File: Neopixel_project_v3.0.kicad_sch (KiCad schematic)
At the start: 67 parts, among them J1 USB_C_Receptacle_USB2.0_16P, J2 Conn_01x02_Pin, Q1 MMBT3904, Q2 MMBT3904, Q3 MMBT3904, Q4 MMBT3904, Q5 DO3407B, Q6 DO3407B, Q7 DO3407B, Q8 DO3407B, SW1 SW_Push, SW2 SW_Push, U1 ESP8685H4, U2 AL8843, U4 USBLC6-4SC6, U5 MC34063AD, Y1 Crystal_GND24

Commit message: changes
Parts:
- removed C1: 100µF, Capacitor_SMD:C_0603_1608Metric, symbol Device:C
- removed C14, C2: 100µF, symbol Device:C
- removed D6: SS34, Diode_SMD:D_SMA, symbol Device:D
- removed SW1, SW2: SW_Push, symbol Switch:SW_Push
- removed U5: MC34063AD, Package_SO:SOIC-8_3.9x4.9mm_P1.27mm, symbol Regulator_Switching:MC34063AD
- added C1, C14, C2: 100µF, Capacitor_SMD:CP_Elec_6.3x7.7, symbol Device:C_Polarized
- added SW1, SW2: TS-1088-AR02016, TS-1088-AR02016:SW_TS-1088_XNP, symbol TS-1088-AR02016:TS-1088-AR02016
- added U3: TD1469, symbol mylibrary:TD1469
- C10, C11, C12, C4, C6, C7, C9: footprint (none) -> Capacitor_SMD:C_0603_1608Metric
- C13: value 7.8µF -> 100nF; footprint (none) -> Capacitor_SMD:C_0603_1608Metric
- C15, C16, C8: footprint (none) -> Capacitor_SMD:C_0805_2012Metric
- C17, C18, C5: footprint (none) -> Capacitor_SMD:C_0402_1005Metric
- C19, C20: footprint (none) -> Capacitor_SMD:C_0402_1005Metric; now not fitted
- C3: footprint Capacitor_SMD:C_0603_1608Metric -> Capacitor_SMD:C_0805_2012Metric
- L1: value 68µ -> 68µH
- L2, L4: footprint (none) -> Inductor_SMD:L_0603_1608Metric
- L3: value 5.6µH -> 22µH; footprint (none) -> Inductor_SMD:L_Ferrocore_DLG-0302
- L5: footprint (none) -> Inductor_SMD:L_0402_1005Metric
- R1, R3, R5, R7: footprint (none) -> Resistor_SMD:R_2010_5025Metric
- R10, R11, R12, R13, R14, R9: footprint (none) -> Resistor_SMD:R_0603_1608Metric
- R15: value 0.333 -> 1M; footprint (none) -> Resistor_SMD:R_0603_1608Metric
- R16: value 2k2 -> 16k; footprint (none) -> Resistor_SMD:R_0603_1608Metric
- R17: value 3k6 -> 5.1k; footprint (none) -> Resistor_SMD:R_0603_1608Metric
- R2, R4, R6, R8: footprint (none) -> Resistor_SMD:R_1206_3216Metric
- U1: footprint (none) -> ESP8685:QFN284X4_EXP
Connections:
- net 24V: now also C1.1, C2.1, U3. (VIN)
- net 3v3: now also R16.2, C14.1; no longer R17.1
- net BOOT: now also SW1.2
- net CHIP_EN: now also SW2.2
- net GND: now also R17.2, C1.2, C14.2, C2.2, SW1.1, SW2.1, U3. (VIN); no longer C13.2, R16.1
- net at R15.2: now also U3. (VIN)
- net at L3.1: now also C13.2, U3. (VIN)
- net at C13.1: now also U3. (VIN)
- new net: R16.1, R17.1, U3. (VIN)
- no-connect marks 11 -> 12
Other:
- note removed: "Tc=4.0 * 10-5 * ton"
- note removed: "Ton=0.195 μs"
- note removed: "Vf=0.55v"
- note removed: "Vout=1.25(1+(R16/R17))"
- moved on the sheet: C11, C12, C15, C16, J1, R10, R13, R14, R9, U4

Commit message: changes
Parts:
- J1: footprint (none) -> Connector_USB:USB_C_Receptacle_G-Switch_GT-USB-7051x
- J2: footprint (none) -> Connector_AMASS:AMASS_XT30UPB-M_1x02_P5.0mm_Vertical
- U3: footprint (none) -> Package_TO_SOT_SMD:TSOT-23-6
- Y1: footprint (none) -> Crystal:Crystal_SMD_Abracon_ABM8AIG-4Pin_3.2x2.5mm
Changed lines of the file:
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@@
 			)
 		)
-		(property "Footprint" ""
+		(property "Footprint" "Package_TO_SOT_SMD:TSOT-23-6"
 			(at 229.87 39.37 0)
 			(effects
@@
 			)
 		)
-		(property "Footprint" ""
+		(property "Footprint" "Crystal:Crystal_SMD_Abracon_ABM8AIG-4Pin_3.2x2.5mm"
 			(at 111.76 172.72 0)
 			(effects
@@
 			)
 		)
-		(property "Footprint" ""
+		(property "Footprint" "Connector_USB:USB_C_Receptacle_G-Switch_GT-USB-7051x"
 			(at 142.24 43.18 0)
 			(effects
@@
 			)
 		)
-		(property "Footprint" ""
+		(property "Footprint" "Connector_AMASS:AMASS_XT30UPB-M_1x02_P5.0mm_Vertical"
 			(at 27.94 82.55 0)
 			(effects

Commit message: snapshot save
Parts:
- removed J1: USB_C_Receptacle_USB2.0_16P, Connector_USB:USB_C_Receptacle_G-Switch_GT-USB-7051x, symbol Connector:USB_C_Receptacle_USB2.0_16P
- removed R13, R14: 5k1, Resistor_SMD:R_0603_1608Metric, symbol Device:R
- added J1: Conn_01x03_Pin, Connector_PinHeader_2.54mm:PinHeader_1x03_P2.54mm_Vertical, symbol Connector:Conn_01x03_Pin
- R1, R3, R5, R7: value 1k -> 1k5; footprint Resistor_SMD:R_2010_5025Metric -> Resistor_SMD:R_1206_3216Metric
- R17: value 5.1k -> 5k1
- R2, R4, R6, R8: footprint Resistor_SMD:R_1206_3216Metric -> Resistor_SMD:R_0805_2012Metric
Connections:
- net 24V: now also U3.5 (VIN); no longer U3. (VIN)
- net GND: now also U3.2 (GND), J1.1 (Pin_1); no longer U3. (VIN)
- net USB_D+: now also J1.3 (Pin_3)
- net USB_D-: now also J1.2 (Pin_2)
- net at R16.1, R17.1: now also U3.3 (FB); no longer U3. (VIN)
- net at C13.2, L3.1: now also U3.6 (SW); no longer U3. (VIN)
- net at R15.2: now also U3.4 (EN); no longer U3. (VIN)
- net at C13.1: now also U3.1 (BST); no longer U3. (VIN)
- no-connect marks 12 -> 8

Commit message: pcb finished
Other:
- note added: "Programming_pins"
- note removed: "usb_connector"
- moved on the sheet: J1, U4
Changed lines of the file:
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@@
 	)
 	(no_connect
-		(at 172.72 53.34)
+		(at 160.02 40.64)
 	)
 	(no_connect
@@
 	)
 	(no_connect
-		(at 175.26 53.34)
+		(at 162.56 40.64)
 	)
 	(no_connect
@@
 	(wire
 		(pts
-			(xy 149.86 50.8) (xy 167.64 50.8)
+			(xy 137.16 38.1) (xy 154.94 38.1)
 		)
 		(stroke
@@
 	(wire
 		(pts
-			(xy 158.75 60.96) (xy 162.56 60.96)
+			(xy 146.05 48.26) (xy 149.86 48.26)
 		)
 		(stroke
@@
 	(wire
 		(pts
-			(xy 149.86 48.26) (xy 170.18 48.26)
+			(xy 137.16 35.56) (xy 157.48 35.56)
 		)
 		(stroke
@@
 	(wire
 		(pts
-			(xy 154.94 45.72) (xy 154.94 39.37)
+			(xy 142.24 33.02) (xy 142.24 26.67)
 		)
 		(stroke
@@
 	(wire
 		(pts
-			(xy 167.64 50.8) (xy 167.64 53.34)
+			(xy 154.94 38.1) (xy 154.94 40.64)
 		)
 		(stroke
@@
 	(wire
 		(pts
-			(xy 158.75 66.04) (xy 158.75 60.96)
+			(xy 146.05 53.34) (xy 146.05 48.26)
 		)
 		(stroke
@@
 	(wire
 		(pts
-			(xy 170.18 48.26) (xy 170.18 53.34)
+			(xy 157.48 35.56) (xy 157.48 40.64)
 		)
 		(stroke
@@
 	(wire
 		(pts
-			(xy 149.86 45.72) (xy 154.94 45.72)
+			(xy 137.16 33.02) (xy 142.24 33.02)
 		)
 		(stroke
@@
 		)
 	)
-	(text "usb_connector"
+	(text "Programming_pins"
 		(exclude_from_sim no)
 		(at 143.764 16.764 0)
@@
 	(global_label "USB_D+"
 		(shape input)
-		(at 167.64 53.34 180)
+		(at 154.94 40.64 180)
 		(fields_autoplaced yes)
 		(effects
@@
 		)
 		(property "Intersheetrefs" "${INTERSHEET_REFS}"
-			(at 157.0348 53.34 0)
+			(at 144.3348 40.64 0)
 			(effects
 				(font
@@
 	(global_label "3v3"
 		(shape input)
-		(at 180.34 60.96 0)
+		(at 167.64 48.26 0)
 		(fields_autoplaced yes)
 		(effects
@@
 		)
 		(property "Intersheetrefs" "${INTERSHEET_REFS}"
-			(at 186.7118 60.96 0)
+			(at 174.0118 48.26 0)
 			(effects
 				(font
@@
 	(global_label "USB_D-"
 		(shape input)
-		(at 170.18 48.26 0)
+		(at 157.48 35.56 0)
 		(fields_autoplaced yes)
 		(effects
@@
 		)
 		(property "Intersheetrefs" "${INTERSHEET_REFS}"
-			(at 180.7852 48.26 0)
+			(at 168.0852 35.56 0)
 			(effects
 				(font
@@
 	(symbol
 		(lib_id "Connector:Conn_01x03_Pin")
-		(at 144.78 48.26 0)
+		(at 132.08 35.56 0)
 		(unit 1)
 		(exclude_from_sim no)
@@
 		(fields_autoplaced yes)
 		(property "Reference" "J1"
-			(at 145.415 40.64 0)
+			(at 132.715 27.94 0)
 			(effects
 				(font
@@
 		)
 		(property "Value" "Conn_01x03_Pin"
-			(at 145.415 43.18 0)
+			(at 132.715 30.48 0)
 			(effects
 				(font
@@
 		)
 		(property "Footprint" "Connector_PinHeader_2.54mm:PinHeader_1x03_P2.54mm_Vertical"
-			(at 144.78 48.26 0)
+			(at 132.08 35.56 0)
 			(effects
 				(font
@@
 		)
 		(property "Datasheet" "~"
-			(at 144.78 48.26 0)
+			(at 132.08 35.56 0)
 			(effects
 				(font
@@
 		)
 		(property "Description" "Generic connector, single row, 01x03, script generated"
-			(at 144.78 48.26 0)
+			(at 132.08 35.56 0)
 			(effects
 				(font
@@
 	(symbol
 		(lib_id "power:GND")
-		(at 158.75 66.04 0)
+		(at 146.05 53.34 0)
 		(unit 1)
 		(exclude_from_sim no)
@@
 		(dnp no)
 		(property "Reference" "#PWR026"
-			(at 158.75 72.39 0)
+			(at 146.05 59.69 0)
 			(effects
 				(font
@@
 		)
 		(property "Value" "GND"
-			(at 160.782 66.294 0)
+			(at 148.082 53.594 0)
 			(effects
 				(font
@@
 		)
 		(property "Footprint" ""
-			(at 158.75 66.04 0)
+			(at 146.05 53.34 0)
 			(effects
 				(font
@@
 		)
 		(property "Datasheet" ""
-			(at 158.75 66.04 0)
+			(at 146.05 53.34 0)
 			(effects
 				(font
@@
 		)
 		(property "Description" "Power symbol creates a global label with name \"GND\" , ground"
-			(at 158.75 66.04 0)
+			(at 146.05 53.34 0)
 			(effects
 				(font
@@
 	(symbol
 		(lib_id "Power_Protection:USBLC6-4SC6")
-		(at 172.72 60.96 270)
+		(at 160.02 48.26 270)
 		(unit 1)
 		(exclude_from_sim no)
@@
 		(dnp no)
 		(property "Reference" "U4"
-			(at 170.18 69.088 90)
+			(at 157.48 56.388 90)
 			(effects
 				(font
@@
 		)
 		(property "Value" "USBLC6-4SC6"
-			(at 165.1 66.802 90)
+			(at 152.4 54.102 90)
 			(effects
 				(font
@@
 		)
 		(property "Footprint" "Package_TO_SOT_SMD:SOT-23-6"
-			(at 162.56 63.5 0)
+			(at 149.86 50.8 0)
 			(effects
 				(font
@@
 		)
 		(property "Datasheet" "https://www.st.com/resource/en/datasheet/usblc6-4.pdf"
-			(at 160.02 63.5 0)
+			(at 147.32 50.8 0)
 			(effects
 				(font
@@
 		)
 		(property "Description" "Very low capacitance ESD protection diode, 4 data-line, SOT-23-6"
-			(at 172.72 60.96 0)
+			(at 160.02 48.26 0)
 			(effects
 				(font
@@
 	(symbol
 		(lib_id "power:GND")
-		(at 154.94 39.37 180)
+		(at 142.24 26.67 180)
 		(unit 1)
 		(exclude_from_sim no)
@@
 		(dnp no)
 		(property "Reference" "#PWR020"
-			(at 154.94 33.02 0)
+			(at 142.24 20.32 0)
 			(effects
 				(font
@@
 		)
 		(property "Value" "GND"
-			(at 152.908 39.116 0)
+			(at 140.208 26.416 0)
 			(effects
 				(font
@@
 		)
 		(property "Footprint" ""
-			(at 154.94 39.37 0)
+			(at 142.24 26.67 0)
 			(effects
 				(font
@@
 		)
 		(property "Datasheet" ""
-			(at 154.94 39.37 0)
+			(at 142.24 26.67 0)
 			(effects
 				(font
@@
 		)
 		(property "Description" "Power symbol creates a global label with name \"GND\" , ground"
-			(at 154.94 39.37 0)
+			(at 142.24 26.67 0)
 			(effects
 				(font

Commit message: pcb and 3d models finished
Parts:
- removed J2: Conn_01x02_Pin, Connector_AMASS:AMASS_XT30UPB-M_1x02_P5.0mm_Vertical, symbol Connector:Conn_01x02_Pin
- added J3: Screw_Terminal_01x02, TerminalBlock_Phoenix:TerminalBlock_Phoenix_MPT-0,5-2-2.54_1x02_P2.54mm_Horizontal, symbol Connector:Screw_Terminal_01x02
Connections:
- net 24V: now also J3.2 (Pin_2)
- net GND: now also J3.1 (Pin_1)
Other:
- note removed: "checklist: - confirm circuit wiring - check available components and cart - make sure no unensesarry components are in the cart - confirm custom schematic symbol pin numbers - confirm footprints - confirm footprint pinouts"
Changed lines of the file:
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@@
 	(wire
 		(pts
-			(xy 33.02 88.9) (xy 33.02 85.09)
-		)
-		(stroke
-			(width 0)
-			(type default)
-		)
-	)
-	(wire
-		(pts
 			(xy 153.67 158.75) (xy 181.61 158.75)
 		)
@@
 	(wire
 		(pts
-			(xy 33.02 82.55) (xy 38.1 82.55)
-		)
-		(stroke
-			(width 0)
-			(type default)
-		)
-	)
-	(wire
-		(pts
 			(xy 196.85 101.6) (xy 213.36 101.6)
 		)
@@
 		)
 	)
-	(text "checklist:\n- confirm circuit wiring\n- check available components and cart\n- make sure no unensesarry components are in the cart\n- confirm custom schematic symbol pin numbers\n- confirm footprints\n- confirm footprint pinouts\n"
-		(exclude_from_sim no)
-		(at 10.16 -34.29 0)
-		(effects
-			(font
-				(size 5.08 5.08)
-			)
-			(justify left)
-		)
-	)
 	(text "led_circuit"
 		(exclude_from_sim no)
@@
 	(global_label "24V"
 		(shape input)
-		(at 38.1 82.55 0)
+		(at 34.29 83.82 0)
 		(fields_autoplaced yes)
 		(effects
@@
 		)
 		(property "Intersheetrefs" "${INTERSHEET_REFS}"
-			(at 44.5928 82.55 0)
+			(at 40.7828 83.82 0)
 			(effects
 				(font
@@
 	(symbol
 		(lib_id "power:GND")
-		(at 33.02 88.9 0)
+		(at 34.29 86.36 0)
 		(unit 1)
 		(exclude_from_sim no)
@@
 		(fields_autoplaced yes)
 		(property "Reference" "#PWR036"
-			(at 33.02 95.25 0)
+			(at 34.29 92.71 0)
 			(effects
 				(font
@@
 		)
 		(property "Value" "GND"
-			(at 33.02 93.98 0)
+			(at 34.29 91.44 0)
 			(effects
 				(font
@@
 		)
 		(property "Footprint" ""
-			(at 33.02 88.9 0)
+			(at 34.29 86.36 0)
 			(effects
 				(font
@@
 		)
 		(property "Datasheet" ""
-			(at 33.02 88.9 0)
+			(at 34.29 86.36 0)
 			(effects
 				(font
@@
 		)
 		(property "Description" "Power symbol creates a global label with name \"GND\" , ground"
-			(at 33.02 88.9 0)
+			(at 34.29 86.36 0)
 			(effects
 				(font
@@
 	)
 	(symbol
+		(lib_id "Connector:Screw_Terminal_01x02")
+		(at 29.21 86.36 180)
+		(unit 1)
+		(exclude_from_sim no)
+		(in_bom yes)
+		(on_board yes)
+		(dnp no)
+		(fields_autoplaced yes)
+		(property "Reference" "J3"
+			(at 29.21 77.47 0)
+			(effects
+				(font
+					(size 1.27 1.27)
+				)
+			)
+		)
+		(property "Value" "Screw_Terminal_01x02"
+			(at 29.21 80.01 0)
+			(effects
+				(font
+					(size 1.27 1.27)
+				)
+			)
+		)
+		(property "Footprint" "TerminalBlock_Phoenix:TerminalBlock_Phoenix_MPT-0,5-2-2.54_1x02_P2.54mm_Horizontal"
+			(at 29.21 86.36 0)
+			(effects
+				(font
+					(size 1.27 1.27)
+				)
+				(hide yes)
+			)
+		)
+		(property "Datasheet" "~"
+			(at 29.21 86.36 0)
+			(effects
+				(font
+					(size 1.27 1.27)
+				)
+				(hide yes)
+			)
+		)
+		(property "Description" "Generic screw terminal, single row, 01x02, script generated (kicad-library-utils/schlib/autogen/connector/)"
+			(at 29.21 86.36 0)
+			(effects
+				(font
+					(size 1.27 1.27)
+				)
+				(hide yes)
+			)
+		)
+		(pin "2"
+		)
+		(pin "1"
+		)
+		(instances
+			(project "Neopixel_project_v3.0"
+				(path "/b6956c8d-1b4a-4d29-b075-b5f8d692fa3c"
+					(reference "J3")
+					(unit 1)
+				)
+			)
+		)
+	)
+	(symbol
 		(lib_id "Transistor_BJT:MMBT3904")
 		(at 151.13 111.76 0)
@@
 					(unit 1)
 				)
-			)
-		)
-	)
-	(symbol
-		(lib_id "Connector:Conn_01x02_Pin")
-		(at 27.94 82.55 0)
-		(unit 1)
-		(exclude_from_sim no)
-		(in_bom yes)
-		(on_board yes)
-		(dnp no)
-		(fields_autoplaced yes)
-		(property "Reference" "J2"
-			(at 28.575 77.47 0)
-			(effects
-				(font
-					(size 1.27 1.27)
-				)
-			)
-		)
-		(property "Value" "Conn_01x02_Pin"
-			(at 28.575 80.01 0)
-			(effects
-				(font
-					(size 1.27 1.27)
-				)
-			)
-		)
-		(property "Footprint" "Connector_AMASS:AMASS_XT30UPB-M_1x02_P5.0mm_Vertical"
-			(at 27.94 82.55 0)
-			(effects
-				(font
-					(size 1.27 1.27)
-				)
-				(hide yes)
-			)
-		)
-		(property "Datasheet" "~"
-			(at 27.94 82.55 0)
-			(effects
-				(font
-					(size 1.27 1.27)
-				)
-				(hide yes)
-			)
-		)
-		(property "Description" "Generic connector, single row, 01x02, script generated"
-			(at 27.94 82.55 0)
-			(effects
-				(font
-					(size 1.27 1.27)
-				)
-				(hide yes)
-			)
-		)
-		(pin "1"
-		)
-		(pin "2"
-		)
-		(instances
-			(project "Neopixel_project_v3.0"
-				(path "/b6956c8d-1b4a-4d29-b075-b5f8d692fa3c"
-					(reference "J2")
-					(unit 1)
-				)

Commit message: added bom.csv and buch of other changes
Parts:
- AE1: now left out of the parts list
- C1, C14, C2: PPU (none) -> 0.0193
- C10, C11, C12, C13, C6, C7, C9: PPU (none) -> 0.0021
- C15, C16, C3: PPU (none) -> 0.1158
- C17, C18: PPU (none) -> 0.0033
- C19, C20: PPU (none) -> 0
- C4: PPU (none) -> 0.0038
- C5, R10, R17, R9: PPU (none) -> 0.0009
- C8: PPU (none) -> 0.0178
- D1: PPU (none) -> 0.069
- D2: PPU (none) -> 0.1638
- D3: PPU (none) -> 0.1589
- D4: PPU (none) -> 0.0962
- D5: PPU (none) -> 0.0265
- J1: PPU (none) -> 0.0105
- J3: PPU (none) -> 0.1513
- L1: PPU (none) -> 0.052
- L2: PPU (none) -> 0.0069
- L3: PPU (none) -> 0.0184
- L4: PPU (none) -> 0.0064
- L5: PPU (none) -> 0.0006
- Q1, Q2, Q3, Q4: PPU (none) -> 0.0095
- Q5, Q6, Q7, Q8: PPU (none) -> 0.0271
- R1, R3, R5, R7: PPU (none) -> 0.013
- R11, R12: value 10k -> 5k1; PPU (none) -> 0.0009
- R15: PPU (none) -> 0.001
- R16: PPU (none) -> 0.0012
- R2, R4, R6, R8: PPU (none) -> 0.0156
- R22: PPU (none) -> 0.0488
- SW1, SW2: PPU (none) -> 0.0415
- U1: PPU (none) -> 1.3435
- U2: PPU (none) -> 0.3568
- U3: PPU (none) -> 0.2999
- U4: PPU (none) -> 0.0273
- Y1: PPU (none) -> 0.0922

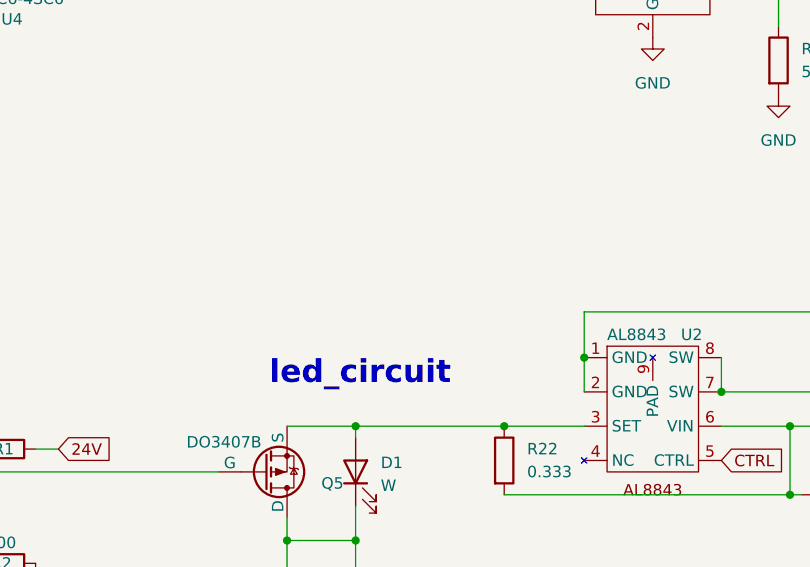
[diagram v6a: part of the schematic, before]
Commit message: added heatsink to bom
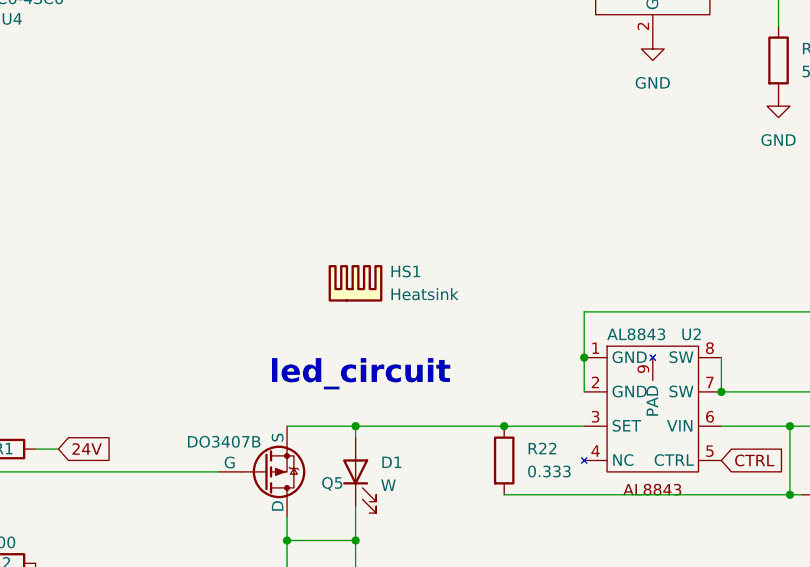
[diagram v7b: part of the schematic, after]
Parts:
- added HS1: Heatsink, 22x22x10, symbol Mechanical:Heatsink
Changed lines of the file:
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@@
+	)
+	(symbol
+		(lib_id "Mechanical:Heatsink")
+		(at 196.85 87.63 0)
+		(unit 1)
+		(exclude_from_sim yes)
+		(in_bom yes)
+		(on_board no)
+		(dnp no)
+		(fields_autoplaced yes)
+		(property "Reference" "HS1"
+			(at 200.66 84.4549 0)
+			(effects
+				(font
+					(size 1.27 1.27)
+				)
+				(justify left)
+			)
+		)
+		(property "Value" "Heatsink"
+			(at 200.66 86.9949 0)
+			(effects
+				(font
+					(size 1.27 1.27)
+				)
+				(justify left)
+			)
+		)
+		(property "Footprint" "22x22x10"
+			(at 197.1548 87.63 0)
+			(effects
+				(font
+					(size 1.27 1.27)
+				)
+				(hide yes)
+			)
+		)
+		(property "Datasheet" "https://www.lcsc.com/datasheet/C286191.pdf"
+			(at 197.1548 87.63 0)
+			(effects
+				(font
+					(size 1.27 1.27)
+				)
+				(hide yes)
+			)
+		)
+		(property "Description" "Heatsink"
+			(at 196.85 87.63 0)
+			(effects
+				(font
+					(size 1.27 1.27)
+				)
+				(hide yes)
+			)
+		)
+		(property "PPU" "0.1324"
+			(at 196.85 87.63 0)
+			(effects
+				(font
+					(size 1.27 1.27)
+				)
+				(hide yes)
+			)
+		)
+		(instances
+			(project "Neopixel_project_v3.0"
+				(path "/b6956c8d-1b4a-4d29-b075-b5f8d692fa3c"
+					(reference "HS1")
+					(unit 1)
+				)
+			)
+		)
 	)
 	(symbol

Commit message: docs
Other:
- title: (none) -> Neopixel project
- moved on the sheet: AE1, C1, C19, C20, C3, D1, D2, D3, D4, D5, HS1, J1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
